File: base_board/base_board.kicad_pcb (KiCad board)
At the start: 6 copper layers, 50 x 50 mm, 53 parts, among them J1 Conn_ARM_JTAG_SWD_20, SW1 SW_Push, U1 STM32F446ZEJx, U2 IS42S16400J-xT, U3 BMI270, U4 USB_C_Receptacle_USB2.0, U5 10p, U6 10p, U7 LD3985M33R_SOT23, Y1 Crystal_GND24

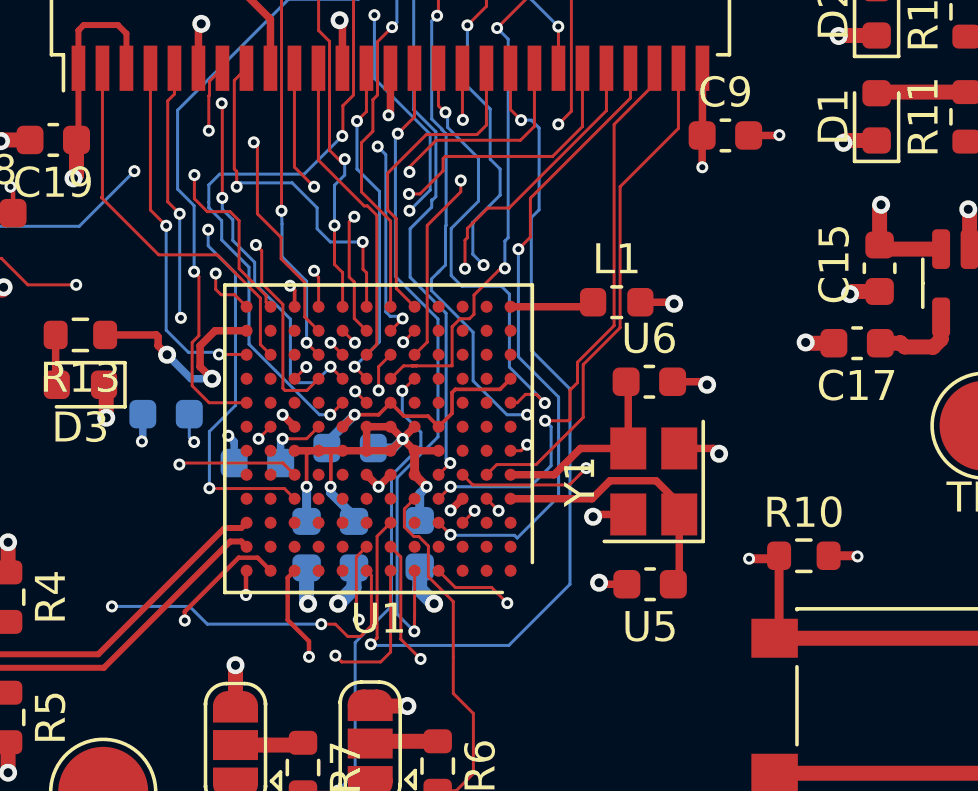
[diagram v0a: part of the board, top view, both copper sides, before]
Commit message: [pcb] added caps for VDDUSB
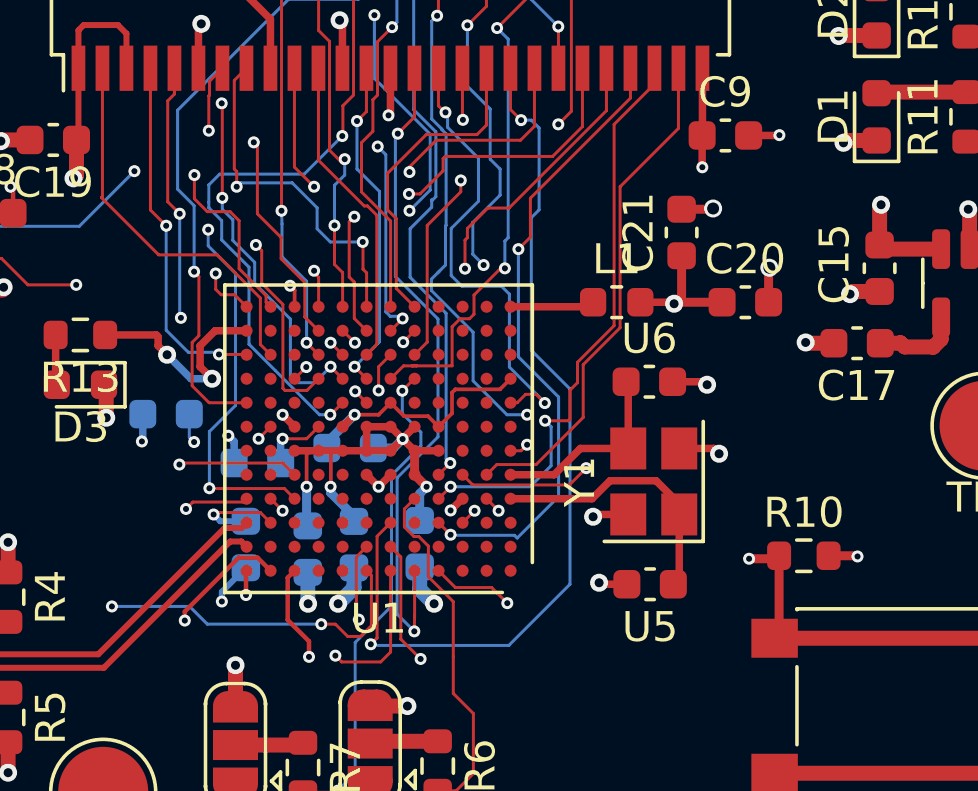
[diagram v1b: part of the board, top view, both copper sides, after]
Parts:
- added C20: 100nF, Capacitor_SMD:C_0603_1608Metric, F.Cu at (139.5, 99.2)
- added C21: 1uF, Capacitor_SMD:C_0603_1608Metric, F.Cu at (137.3, 96.9)
- added C22: 100nF, Capacitor_SMD:C_0603_1608Metric, B.Cu at (122.8, 107.3)
- moved C1 0.16 mm to (124.9, 107.5)
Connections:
- U1 pad C11: Net-(U1-VDDA) -> +3V3
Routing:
- net +3V3: track 72.0 -> 78.7 mm, vias 23 -> 24
- net GND: track 76.7 -> 80.2 mm, vias 49 -> 52
- net /USART1_TX: track 0.00 -> 2.16 mm, vias 0 -> 1
- net /USART1_RX: track 0.00 -> 0.57 mm, vias 0 -> 1

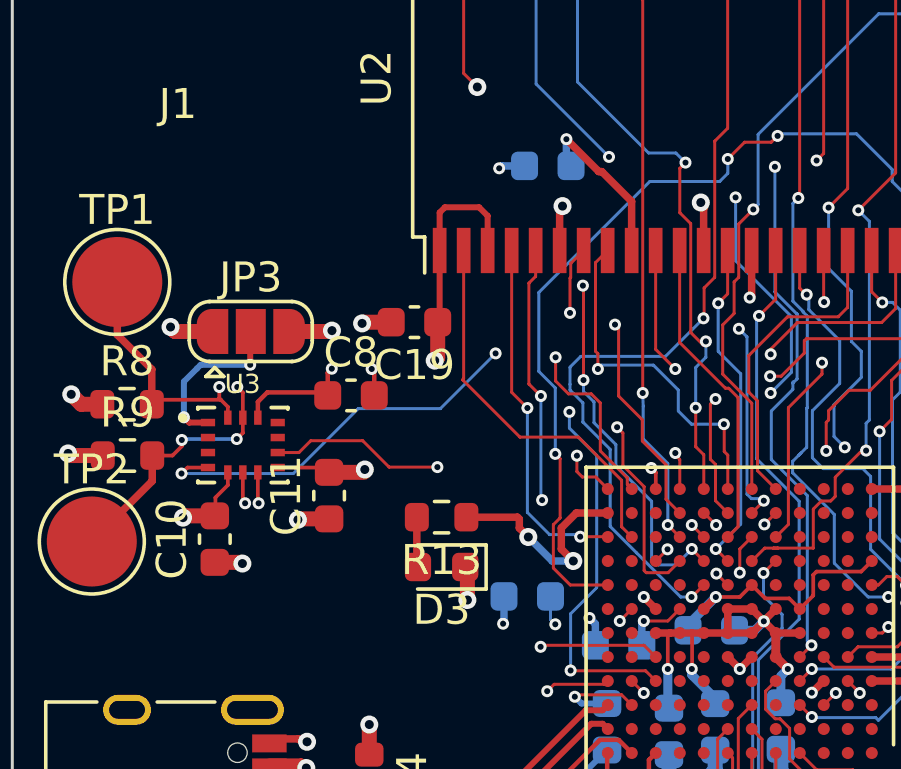
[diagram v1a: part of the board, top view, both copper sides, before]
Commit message: [pcb] draft length matching
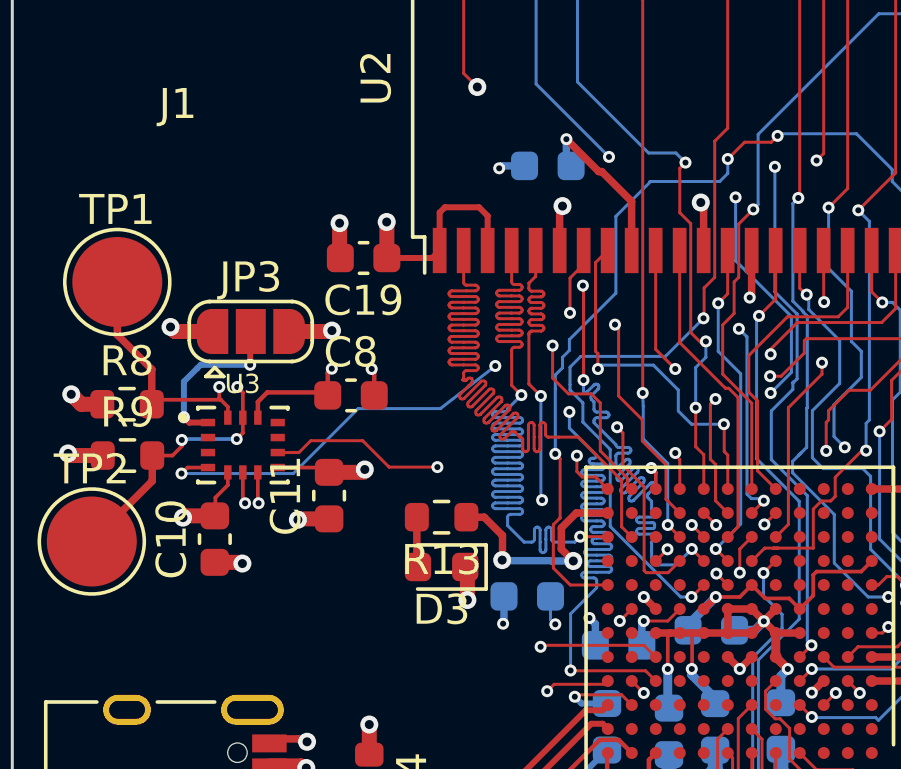
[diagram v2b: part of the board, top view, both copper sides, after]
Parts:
- moved C19 2.73 mm to (114.7, 91.7)
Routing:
- net /FMC_D1: track 12.0 -> 39.9 mm
- net /FMC_D0: track 13.0 -> 39.7 mm
- net /FMC_D3: track 17.9 -> 40.7 mm
- net /FMC_D2: track 17.5 -> 39.5 mm
- net /FMC_D9: track 29.4 -> 40.0 mm
- net +3V3: track 78.7 -> 78.0 mm

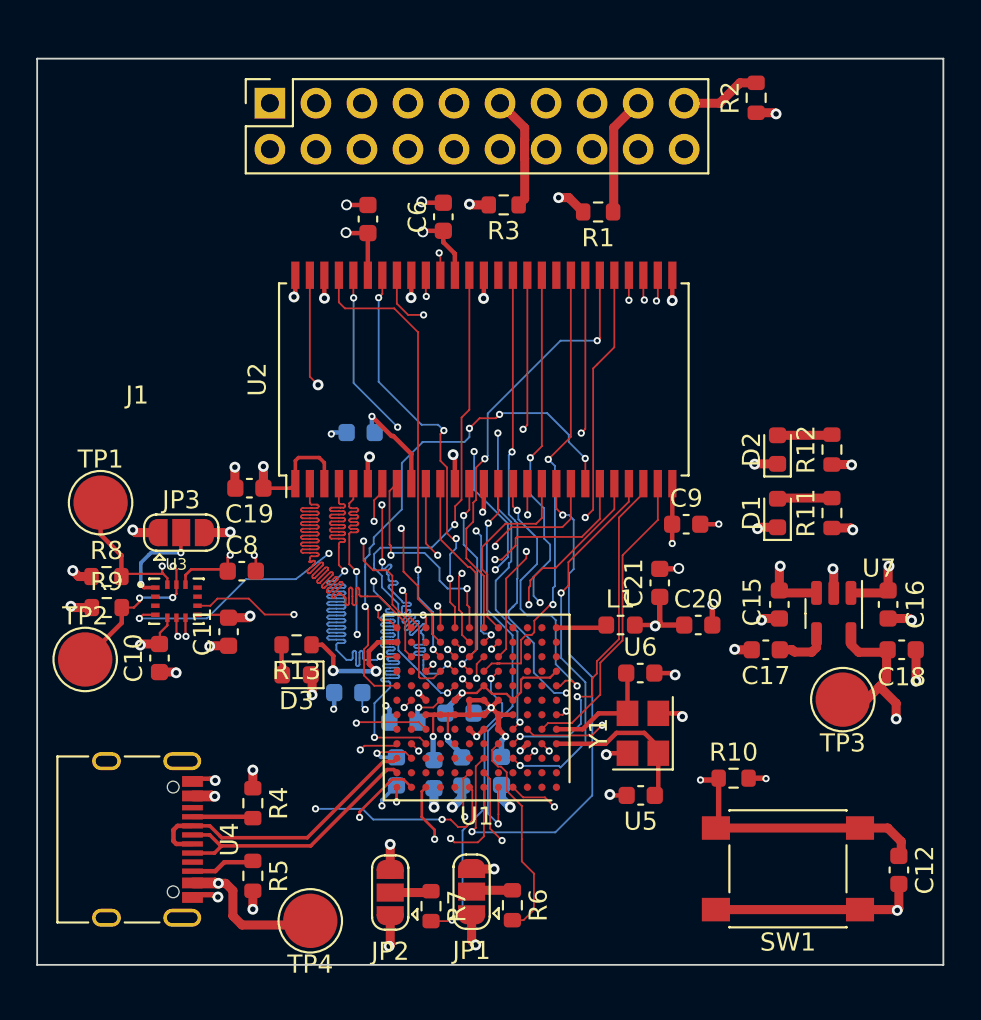
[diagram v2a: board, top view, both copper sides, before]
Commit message: [pcb] fixed length matching for sdram memory
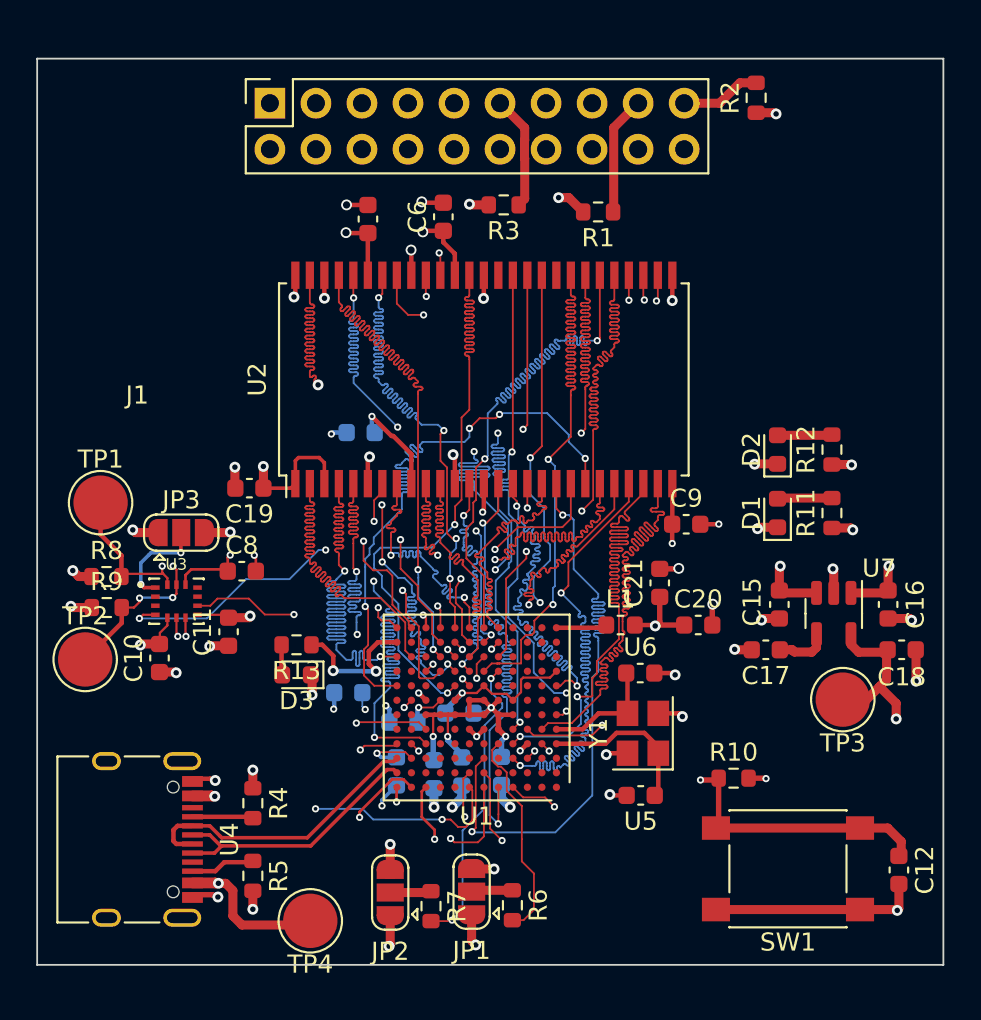
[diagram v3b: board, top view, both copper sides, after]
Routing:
- net /FMC_A3: track 17.0 -> 34.9 mm
- net /FMC_A10: track 17.2 -> 35.1 mm
- net /FMC_D13: track 22.3 -> 37.8 mm
- net /FMC_D0: track 39.7 -> 24.4 mm
- net /FMC_A1: track 21.2 -> 35.7 mm
- net /FMC_A0: track 17.9 -> 32.3 mm
- net /FMC_A2: track 19.5 -> 33.5 mm
- net /FMC_D12: track 22.5 -> 35.9 mm
- net /FMC_D11: track 23.2 -> 36.3 mm
- net /FMC_D10: track 23.3 -> 35.9 mm
- net /FMC_A8: track 24.1 -> 36.6 mm
- net /FMC_A7: track 24.5 -> 36.4 mm
- net /FMC_A11: track 25.5 -> 36.5 mm
- net /FMC_SDNWE: track 15.5 -> 26.5 mm
- net /FMC_D14: track 25.0 -> 35.9 mm
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
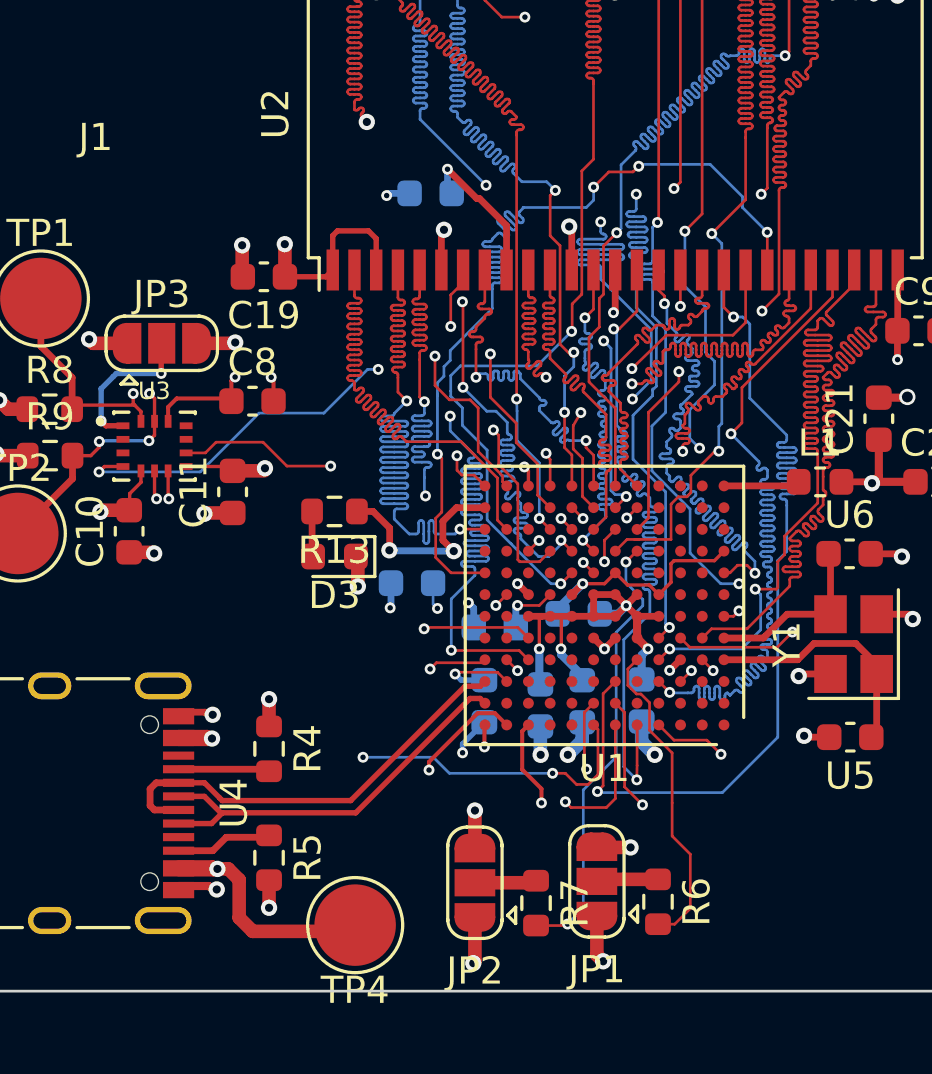
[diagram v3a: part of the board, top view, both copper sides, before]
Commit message: [pcb] fixed power planes. Fixed traces shape
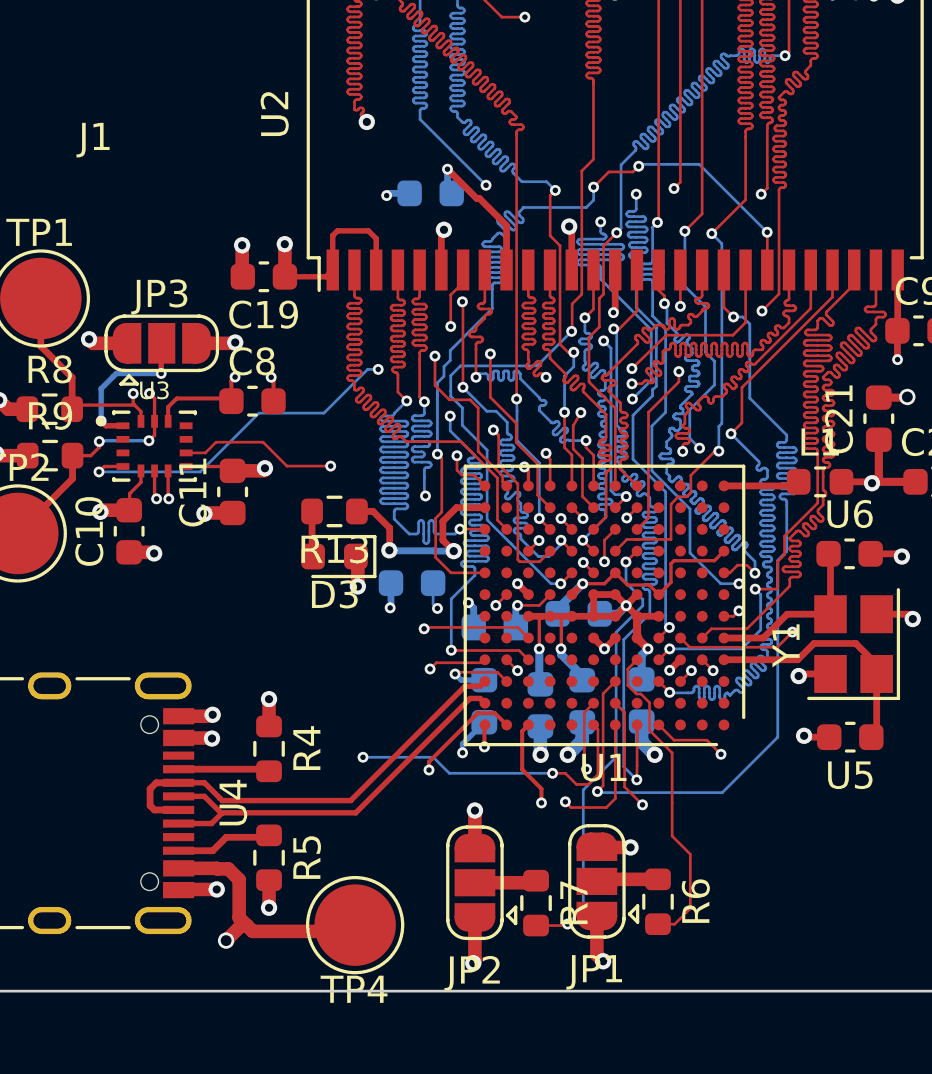
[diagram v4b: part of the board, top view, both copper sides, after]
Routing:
- net /RESET: track 71.7 -> 64.1 mm
- net /SWDIO: track 64.5 -> 60.3 mm
- net +5V: track 20.6 -> 18.7 mm
- added copper zone on In3.Cu, net +5V
- added copper zone on In4.Cu, net GND
- removed copper zone on In4.Cu, net +5V
- removed copper zone on In3.Cu, net GND

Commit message: [pcb] added review corrections
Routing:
- net /FMC_A0: track 32.3 -> 21.5 mm
- net /SWO: track 70.9 -> 66.5 mm
- net +3V3: track 78.0 -> 76.8 mm
- net /FMC_A6: track 36.2 -> 35.7 mm

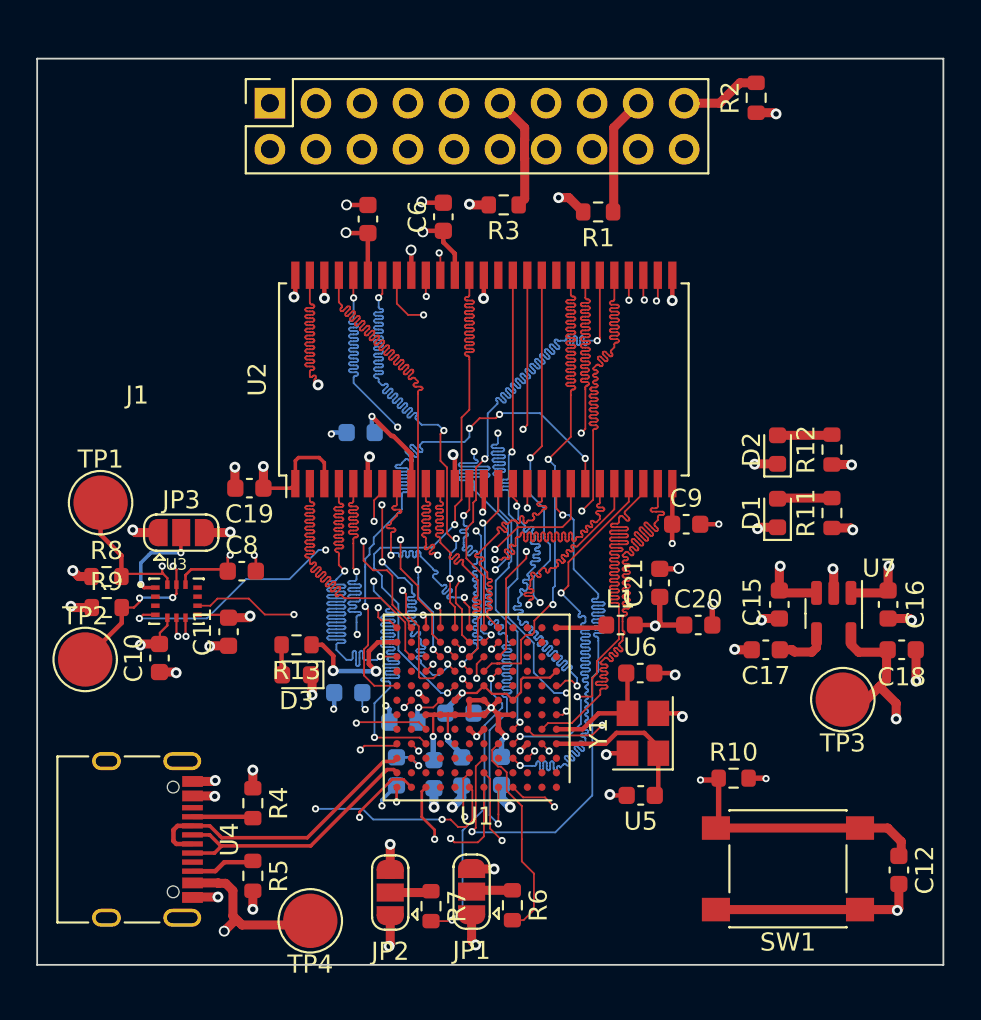
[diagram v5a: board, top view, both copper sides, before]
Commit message: [pcb] added M3 holes
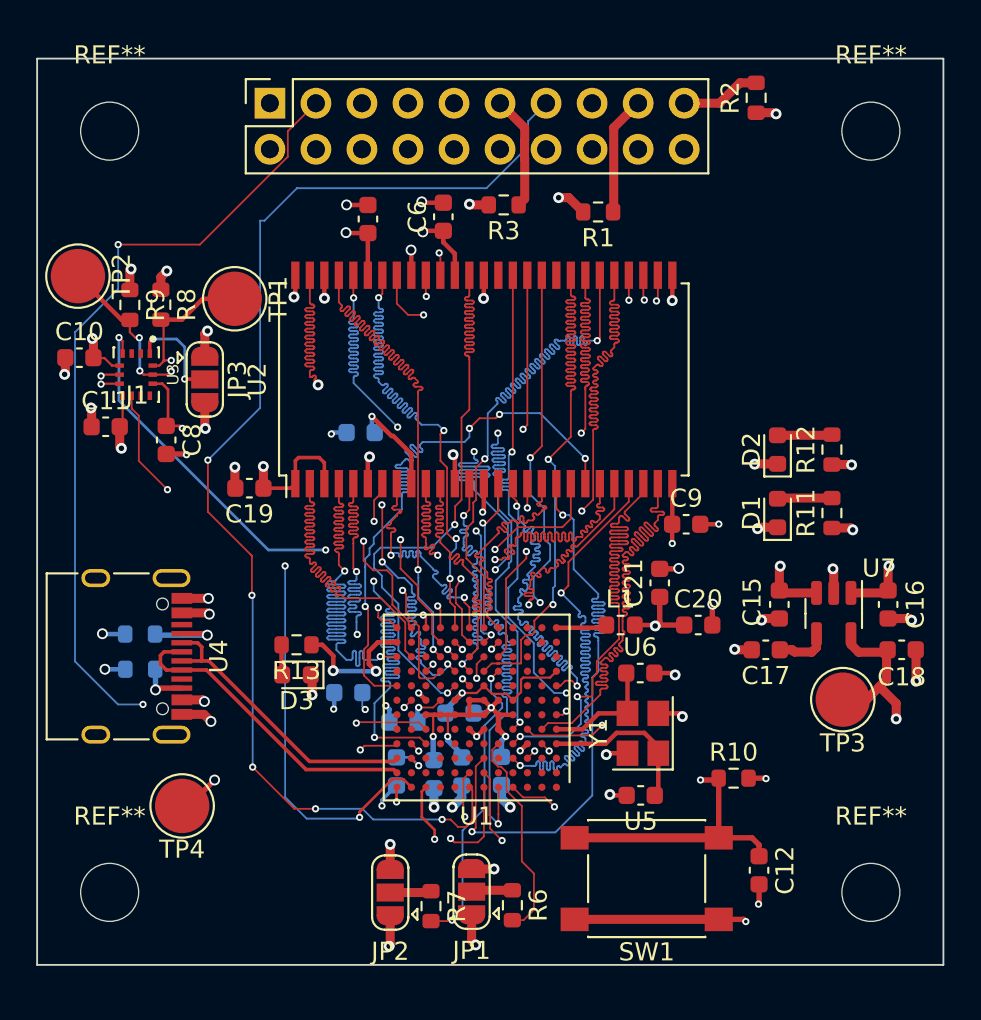
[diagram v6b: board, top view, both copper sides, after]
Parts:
- added REF**: MountingHole_3.2mm_M3, MountingHole:MountingHole_3.2mm_M3, F.Cu at (149.0, 72.0)
- added REF**: MountingHole_3.2mm_M3, MountingHole:MountingHole_3.2mm_M3, F.Cu at (149.0, 114.0)
- added REF**: MountingHole_3.2mm_M3, MountingHole:MountingHole_3.2mm_M3, F.Cu at (107.0, 72.0)
- added REF**: MountingHole_3.2mm_M3, MountingHole:MountingHole_3.2mm_M3, F.Cu at (107.0, 114.0)
- R4, R5: moved to B.Cu
- moved TP2 21.2 mm to (105.2, 80.0), turned to -90 degrees
- moved C10 17.1 mm to (105.3, 84.5), turned to 0 degrees
- moved R9 16.7 mm to (108.1, 81.6), turned to -90 degrees
- moved R8 15.3 mm to (109.8, 81.6), turned to -90 degrees
- moved TP1 13.5 mm to (113.9, 81.2), turned to -90 degrees
- moved C11 13.2 mm to (106.8, 88.3), turned to 0 degrees
- moved R5 13.0 mm to (108.7, 101.7), turned to 180 degrees
- moved U3 12.7 mm to (108.5, 85.4), turned to -90 degrees
- moved R4 11.2 mm to (108.7, 99.8), turned to 0 degrees
- moved U4 10.1 mm to (107.3, 101.0)
- moved TP4 9.50 mm to (111.0, 109.2)
- moved JP3 8.55 mm to (112.2, 85.7), turned to -90 degrees
- moved C8 8.36 mm to (110.1, 89.0), turned to -90 degrees
- moved SW1 7.81 mm to (136.6, 113.2)
- moved C12 7.71 mm to (142.8, 112.8)
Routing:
- net /BMI270_SDA: track 25.1 -> 39.1 mm
- net /BMI270_INT2: track 12.6 -> 22.5 mm
- net /BMI270_SCL: track 25.8 -> 33.4 mm
- net /SWCLK: track 61.5 -> 54.7 mm, vias 1 -> 2
- net /BMI270_INT1: track 21.4 -> 27.9 mm
- net +5V: track 18.7 -> 13.3 mm, vias 5 -> 6
- net /TRST: track 66.5 -> 71.1 mm, vias 1 -> 3
- net /SWDIO: track 60.3 -> 57.4 mm
- net /USB_D+: track 15.1 -> 17.3 mm
- net /TDI: track 64.1 -> 62.8 mm
- net Net-(U4-CC1): track 3.36 -> 4.35 mm, vias 0 -> 1
- net Net-(U4-CC2): track 3.56 -> 2.64 mm, vias 0 -> 1
- net /SWO: track 66.5 -> 67.3 mm, vias 2 -> 5
- net GND: track 80.7 -> 80.6 mm, vias 52 -> 53
